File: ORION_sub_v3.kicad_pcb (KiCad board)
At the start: 2 copper layers, 45 x 72 mm, 74 parts, among them J1 Conn_01x02, J10 Conn_01x01, J11 Conn_01x05, J12 Conn_01x04, J2 Conn_01x03, J3 Conn_01x04, J4 Conn_01x02, J5 Conn_01x01, J6 Conn_01x04, J7 Conn_01x03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

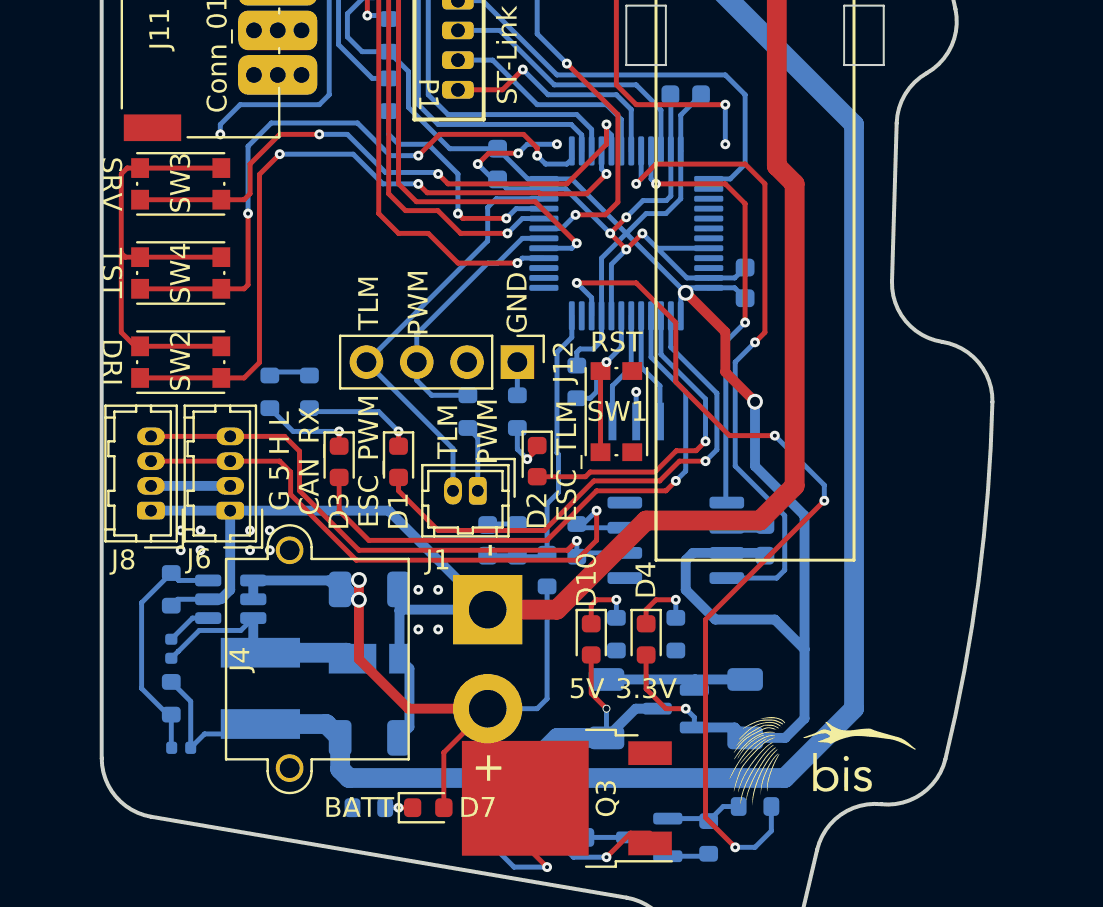
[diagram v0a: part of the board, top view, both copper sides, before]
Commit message: スイッチ変更、電源ヒューズ追加
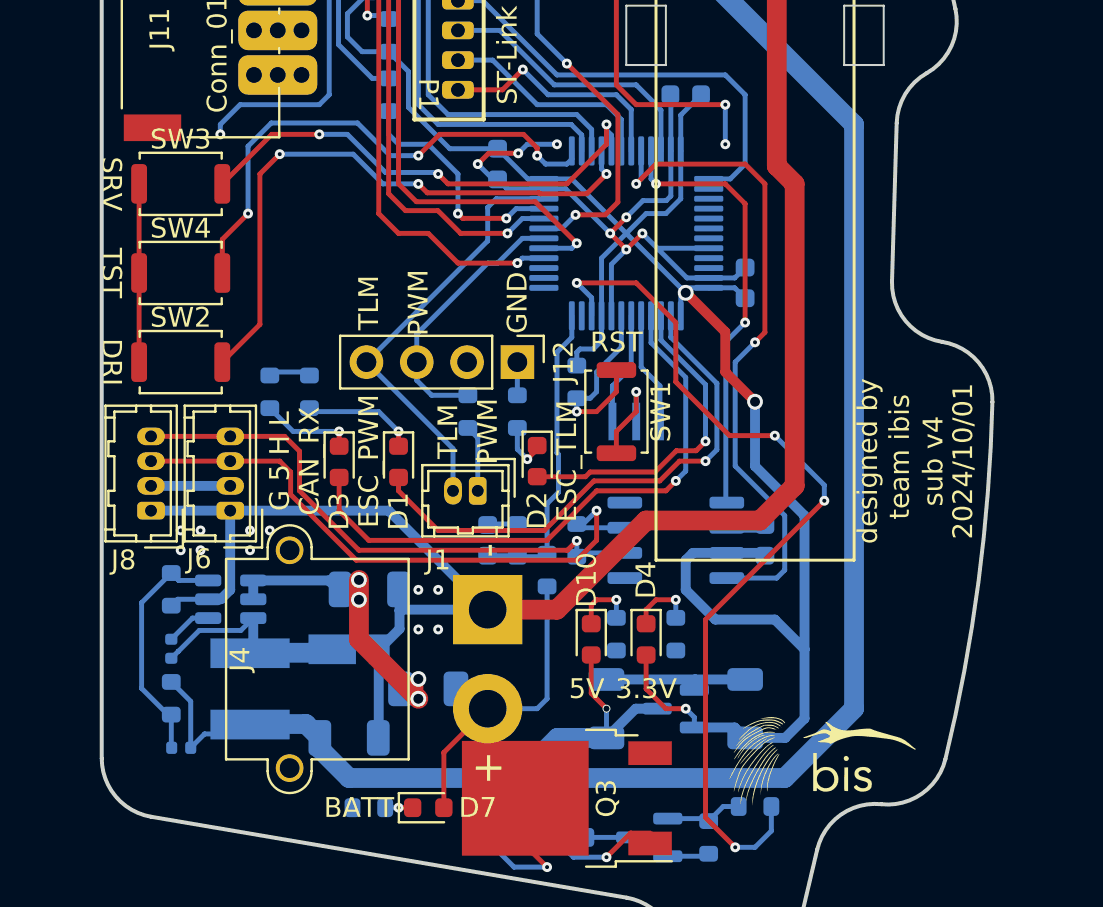
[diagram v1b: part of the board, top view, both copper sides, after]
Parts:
- added F1: Polyfuse, Fuse:Fuse_1206_3216Metric, B.Cu at (110.0, 101.0)
- SW1, SW2, SW3, SW4: footprint Button_Switch_SMD:SW_Push_1P1T_NO_CK_KMR2 -> Button_Switch_SMD:SW_Push_SPST_NO_Alps_SKRK
- moved D9 1.13 mm to (106.0, 99.0)
- moved C13 1.03 mm to (106.0, 103.5)
- moved L1 0.53 mm to (101.0, 101.0)
- turned SW1 to -90 degrees
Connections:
- C12 pad 1: +BATT -> /BATT_fuse
- U4 pad 4: +BATT -> /BATT_fuse
- U4 pad 5: +BATT -> /BATT_fuse
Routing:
- net +BATT: track 41.3 -> 23.0 mm, vias 3 -> 1
- net /BATT_fuse: track 0.00 -> 17.0 mm, vias 0 -> 4
- net GND: track 234.3 -> 223.2 mm, vias 23 -> 22
- net /SW_2: track 31.9 -> 26.3 mm
- net /SW_0: track 36.3 -> 30.7 mm
- net /SW_1: track 30.1 -> 24.7 mm
- net +5V: track 103.5 -> 102.9 mm
- net Net-(C3-Pad1): track 11.7 -> 11.1 mm
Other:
- board text added: "2024/10/01"
- board text added: "sub v4"
- board text removed: "2024/01/09"
- board text removed: "sub v3"

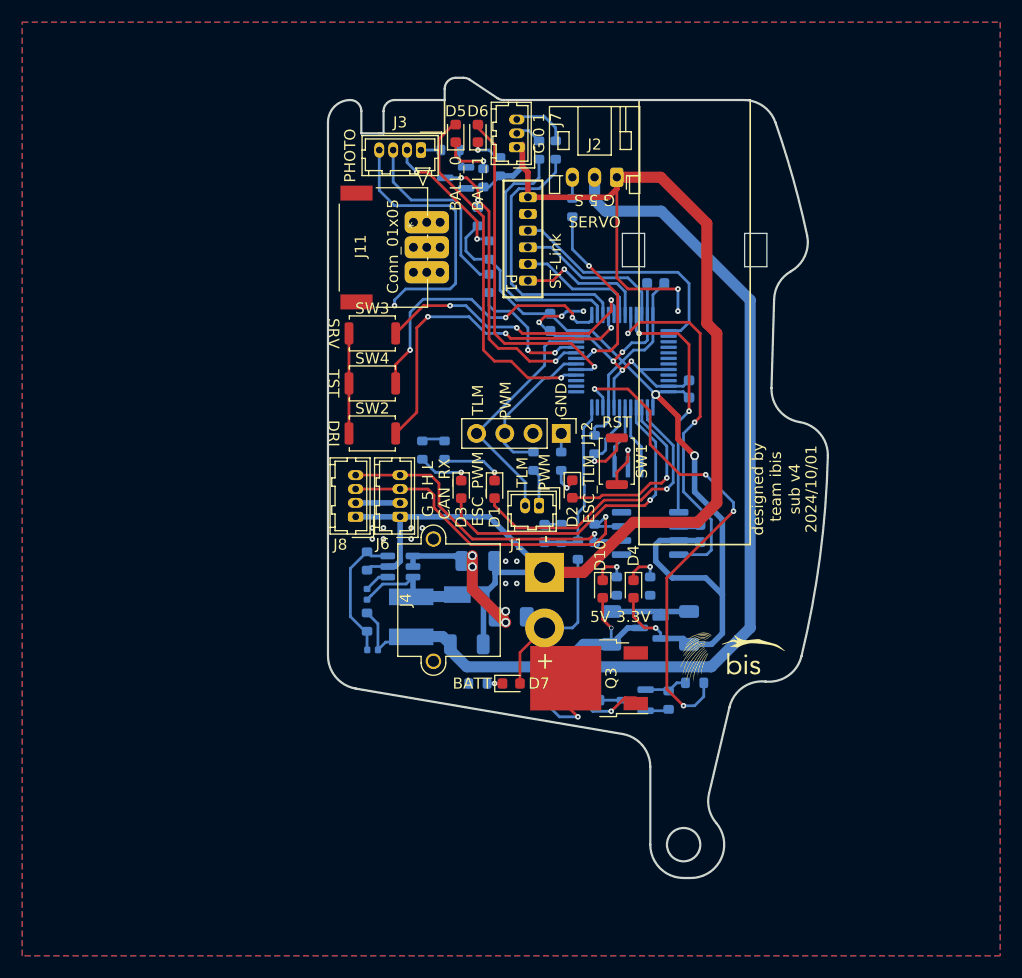
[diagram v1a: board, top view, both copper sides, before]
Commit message: KiCAD8.0に更新
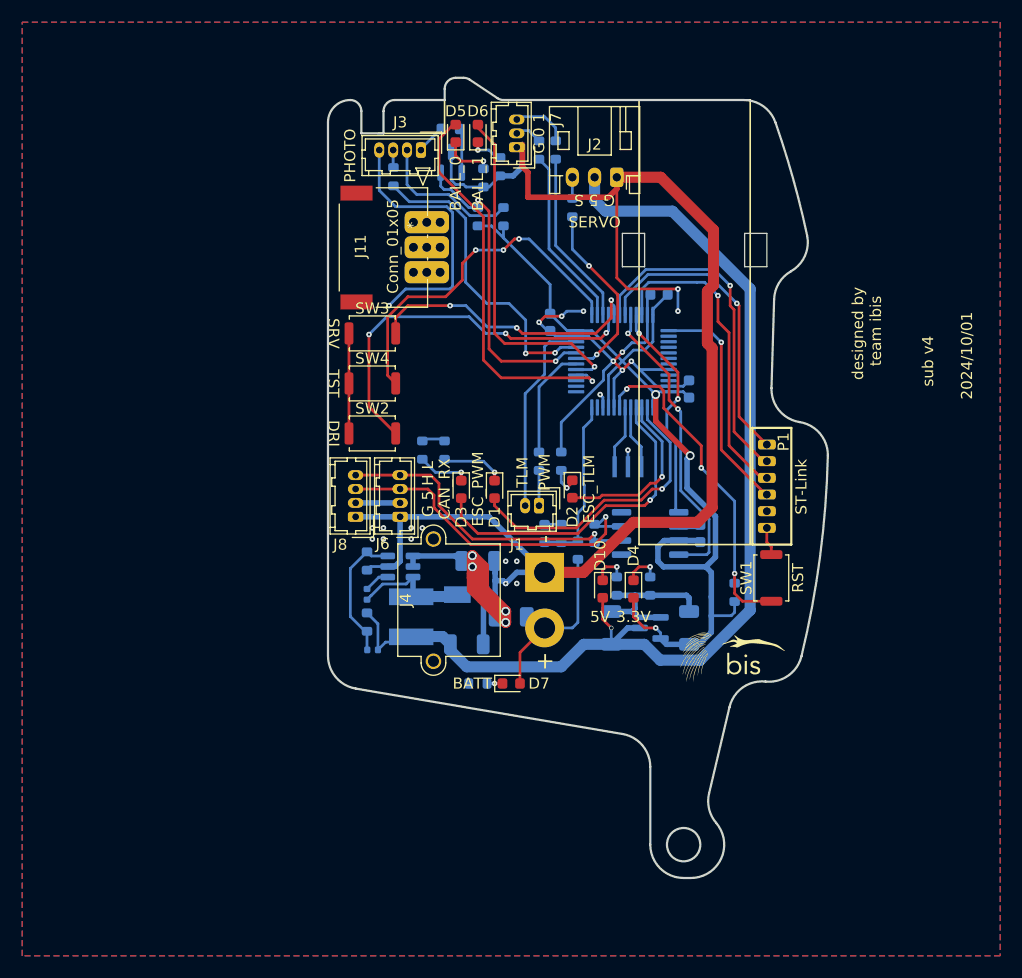
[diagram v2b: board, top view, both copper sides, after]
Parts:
- removed J12: Conn_01x04, Connector_PinHeader_2.54mm:PinHeader_1x04_P2.54mm_Vertical
- removed Q2: Q_NMOS_GSD, Package_TO_SOT_SMD:SOT-23
- removed Q3: Q_NMOS_GDS, Package_TO_SOT_SMD:TO-252-2
- removed R23, R24, R25, R26: 1k, Resistor_SMD:R_0603_1608Metric
- Q1: value Q_NPN_BCE -> Q_NPN_BEC
- moved P1 36.7 mm to (133.0, 93.0), turned to 90 degrees
- moved R1 18.3 mm to (130.1, 98.8), turned to 90 degrees
- moved SW1 17.4 mm to (133.4, 97.5), turned to 90 degrees
- moved R18 12.9 mm to (99.4, 61.4)
- moved R20 3.27 mm to (109.3, 65.0)
- moved R21 1.90 mm to (104.5, 57.1)
- moved Q1 1.46 mm to (104.6, 60.1), turned to 90 degrees
- moved C2 1.04 mm to (123.3, 72.0)
- moved R19 0.50 mm to (112.5, 87.0)
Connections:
- Q1 pad 2: GND -> /INTALAPTER_OUT
- Q1 pad 3: /INTALAPTER_OUT -> GND
- U1 pad 10: /ESC_SW -> unconnected-(U1-Pad10)
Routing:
- net /ESC_SW: track 45.3 -> 0.00 mm, vias 4 -> 0
- net /NRST: track 9.68 -> 30.8 mm, vias 1 -> 3
- net /USART_TX: track 11.1 -> 30.6 mm, vias 0 -> 1
- net GND: track 223.2 -> 239.2 mm
- net Net-(J3-Pad3): track 17.5 -> 1.59 mm
- net /LED_SW: track 12.1 -> 28.0 mm
- net /USART_RX: track 12.1 -> 27.4 mm
- net /SWDIO: track 14.0 -> 28.4 mm, vias 0 -> 1
- net +BATT: track 23.0 -> 14.8 mm, vias 1 -> 0
- net /PHOTO_1: track 24.0 -> 15.8 mm
- net /BATT_fuse: track 17.0 -> 25.1 mm
- net Net-(Q3-Pad1): track 7.64 -> 0.00 mm, vias 1 -> 0
- net /PHOTO_0: track 23.6 -> 16.2 mm
- net /CAN_RX: track 33.3 -> 27.3 mm
- net +3.3V: track 96.7 -> 90.7 mm
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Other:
- board text removed: "GND"

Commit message: OLED追加
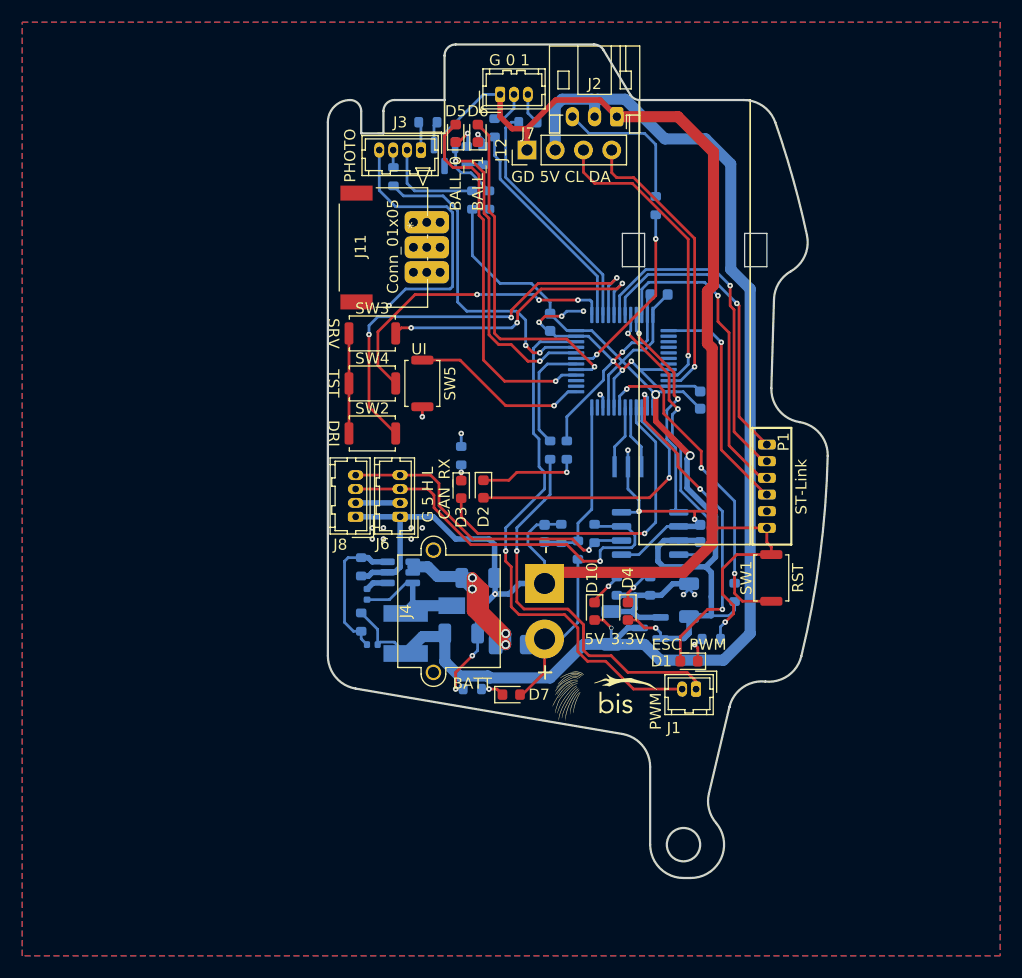
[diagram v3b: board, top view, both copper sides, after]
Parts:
- added J12: Conn_01x04, Connector_PinHeader_2.54mm:PinHeader_1x04_P2.54mm_Vertical, F.Cu at (111.4, 59.0)
- added SW5: SW_Push, Button_Switch_SMD:SW_Push_SPST_NO_Alps_SKRK, F.Cu at (102.0, 80.0)
- moved R5 29.4 mm to (128.0, 103.0), turned to 180 degrees
- moved D1 23.4 mm to (126.0, 105.0), turned to 180 degrees
- moved J1 21.7 mm to (126.6, 107.5)
- moved LG1 12.0 mm to (118.5, 108.0)
- moved LG2 12.0 mm to (118.5, 108.0)
- moved D2 8.00 mm to (107.5, 89.5)
- moved R14 7.50 mm to (123.0, 64.0)
- moved J2 5.45 mm to (119.5, 56.0)
- moved J7 4.98 mm to (109.0, 54.0), turned to 0 degrees
- moved R3 4.47 mm to (108.5, 57.0)
- moved R4 3.54 mm to (111.5, 56.5), turned to 180 degrees
- moved R7 3.54 mm to (105.5, 86.5)
- moved R20 3.18 mm to (106.5, 63.5)
- moved C8 2.50 mm to (126.0, 99.5)
- moved F1 2.50 mm to (110.0, 103.5)
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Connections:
- U1 pad 13: unconnected-(U1-Pad13) -> /SW_3
- U1 pad 45: unconnected-(U1-Pad45) -> /LCD_I2C_SCL
- U1 pad 46: unconnected-(U1-Pad46) -> /LCD_I2C_SDA
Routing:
- net GND: track 239.2 -> 279.3 mm, vias 22 -> 26
- net Net-(J1-Pin_1): track 3.17 -> 35.7 mm, vias 0 -> 1
- net /ESC_TLM: track 18.1 -> 49.1 mm, vias 0 -> 1
- net /LCD_I2C_SCL: track 0.00 -> 27.3 mm, vias 0 -> 1
- net /LCD_I2C_SDA: track 0.00 -> 26.3 mm, vias 0 -> 1
- net +5V: track 98.4 -> 117.6 mm
- net /SW_3: track 0.00 -> 16.1 mm, vias 0 -> 1
- net Net-(J2-Pin_3): track 1.90 -> 13.2 mm
- net /LED_1: track 15.8 -> 24.8 mm
- net Net-(D2-K): track 2.68 -> 8.97 mm
- net /PHOTO_1: track 15.8 -> 21.8 mm
- net /SW_2: track 32.0 -> 27.4 mm
- net /INTALAPTER_OUT: track 28.5 -> 32.8 mm
- net /SW_0: track 34.6 -> 38.9 mm
- net Net-(J3-Pin_2): track 13.2 -> 9.15 mm
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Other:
- board size 45 x 72 mm -> 45 x 75 mm
- board text added: "2024/11/20"
- board text added: "GD 5V CL DA"
- board text added: "UI"
- board text removed: "2024/10/01"
- board text removed: "ESC_TLM"
- board text removed: "G 5 S"
- board text removed: "SERVO"
- board text removed: "TLM"

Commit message: 発注
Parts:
- Q1: value Q_NPN_BEC -> 2SC4213
- moved Q1 1.12 mm to (104.5, 60.5)
- moved R11 1.12 mm to (107.0, 60.0)
- moved R12 1.12 mm to (108.5, 60.0)
- moved R3 0.71 mm to (109.0, 56.5)
- moved R21 0.50 mm to (102.5, 57.0)
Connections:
- Q1 pad 2: /INTALAPTER_OUT -> GND
- Q1 pad 3: GND -> /INTALAPTER_OUT
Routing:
- net GND: track 279.3 -> 272.6 mm
- net /INTALAPTER_OUT: track 32.8 -> 28.7 mm
- net /LED_3: track 33.4 -> 32.4 mm
- net Net-(D6-K): track 1.97 -> 2.88 mm
- net Net-(D5-K): track 2.61 -> 3.46 mm
- net /PHOTO_1: track 21.8 -> 21.0 mm
- net Net-(J7-Pin_2): track 3.38 -> 2.68 mm
- net /SW_0: track 38.9 -> 38.2 mm
- net +5V: track 117.6 -> 118.2 mm
- net Net-(J3-Pin_1): track 2.58 -> 2.08 mm

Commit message: 更新
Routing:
- net unconnected-(U1-PA0-Pad10): track 1.27 -> 0.00 mm, vias 1 -> 0
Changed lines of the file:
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@@
 	)
 	(segment
-		(start 126.625 107.5)
-		(end 126.625 106.8)
+		(start 116.5 101.7)
+		(end 116.5 104)
+		(width 0.25)
+		(layer "F.Cu")
+		(net 39)
+	)
+	(segment
+		(start 115.1 100.3)
+		(end 116.5 101.7)
+		(width 0.25)
+		(layer "F.Cu")
+		(net 39)
+	)
+	(segment
+		(start 110.5 99.65)
+		(end 111.15 100.3)
+		(width 0.25)
+		(layer "F.Cu")
+		(net 39)
+	)
+	(segment
+		(start 116.5 104)
+		(end 117 104.5)
+		(width 0.25)
+		(layer "F.Cu")
+		(net 39)
+	)
+	(segment
+		(start 119 104.5)
+		(end 120.5 106)
+		(width 0.25)
+		(layer "F.Cu")
+		(net 39)
+	)
+	(segment
+		(start 126.625 106.8)
+		(end 126.625 107.5)
+		(width 0.25)
+		(layer "F.Cu")
+		(net 39)
+	)
+	(segment
+		(start 117 104.5)
+		(end 119 104.5)
 		(width 0.25)
 		(layer "F.Cu")
@@
 	)
 	(segment
+		(start 120.5 106)
+		(end 125.825 106)
+		(width 0.25)
+		(layer "F.Cu")
+		(net 39)
+	)
+	(segment
 		(start 111.15 100.3)
 		(end 115.1 100.3)
@@
 	)
 	(segment
-		(start 126.625 106.8)
-		(end 125.825 106)
-		(width 0.25)
-		(layer "F.Cu")
-		(net 39)
-	)
-	(segment
-		(start 116.5 101.7)
-		(end 116.5 102.5)
-		(width 0.25)
-		(layer "F.Cu")
-		(net 39)
-	)
-	(segment
-		(start 116.5 104)
-		(end 117 104.5)
-		(width 0.25)
-		(layer "F.Cu")
-		(net 39)
-	)
-	(segment
-		(start 116.5 102.5)
-		(end 116.5 102.363604)
-		(width 0.25)
-		(layer "F.Cu")
-		(net 39)
-	)
-	(segment
-		(start 110.5 99.65)
-		(end 111.15 100.3)
-		(width 0.25)
-		(layer "F.Cu")
-		(net 39)
-	)
-	(segment
-		(start 116.5 102.363604)
-		(end 116.5 102)
-		(width 0.25)
-		(layer "F.Cu")
-		(net 39)
-	)
-	(segment
-		(start 116.5 102.5)
-		(end 116.5 104)
-		(width 0.25)
-		(layer "F.Cu")
-		(net 39)
-	)
-	(segment
-		(start 115.1 100.3)
-		(end 116.5 101.7)
-		(width 0.25)
-		(layer "F.Cu")
-		(net 39)
-	)
-	(segment
 		(start 125.825 106)
-		(end 120.5 106)
-		(width 0.25)
-		(layer "F.Cu")
-		(net 39)
-	)
-	(segment
-		(start 117 104.5)
-		(end 119 104.5)
-		(width 0.25)
-		(layer "F.Cu")
-		(net 39)
-	)
-	(segment
-		(start 120.5 106)
-		(end 119 104.5)
+		(end 126.625 106.8)
 		(width 0.25)
 		(layer "F.Cu")
@@
 		(net 57)
 	)
-	(via
-		(at 118 81)
-		(size 0.5)
-		(drill 0.2)
-		(layers "F.Cu" "B.Cu")
-		(net 66)
-	)
-	(segment
-		(start 118.25 81.25)
-		(end 118.25 82.1625)
-		(width 0.25)
-		(layer "B.Cu")
-		(net 66)
-	)
-	(segment
-		(start 118 81)
-		(end 118.25 81.25)
-		(width 0.25)
-		(layer "B.Cu")
-		(net 66)
-	)
-	(segment
+	(segment
